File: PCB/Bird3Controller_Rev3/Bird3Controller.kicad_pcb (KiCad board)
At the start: 2 copper layers, 43 x 108 mm, 69 parts, among them IC1 M24C08-RMN6TP, IC2 AP63203WU-7, J1 Bird 3 24-pin Connector, J2 TXW154028S0 Connector, J3 87832-2220, J4 Adafruit USB-C Breakout, Q1 2N7002A, SW1 SW_Boot, SW2 SW_Reset, U1 ESP32-S3-WROOM-1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

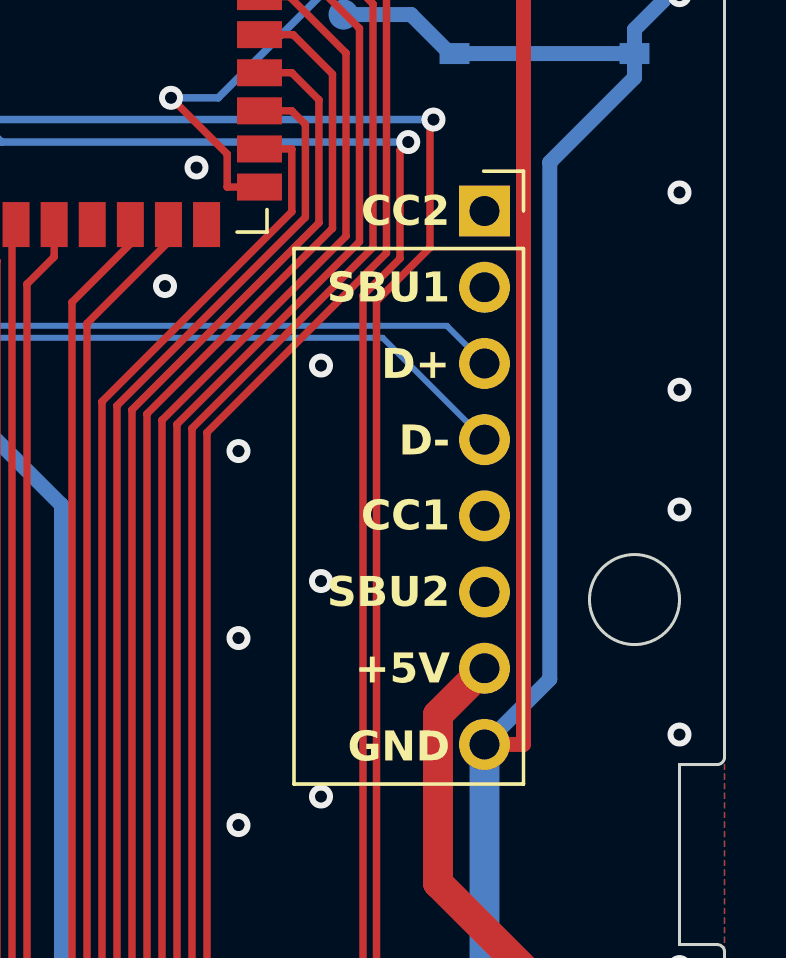
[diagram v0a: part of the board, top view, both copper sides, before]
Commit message: Add `Rating` field, use lower cost VIN cap, add description to most components
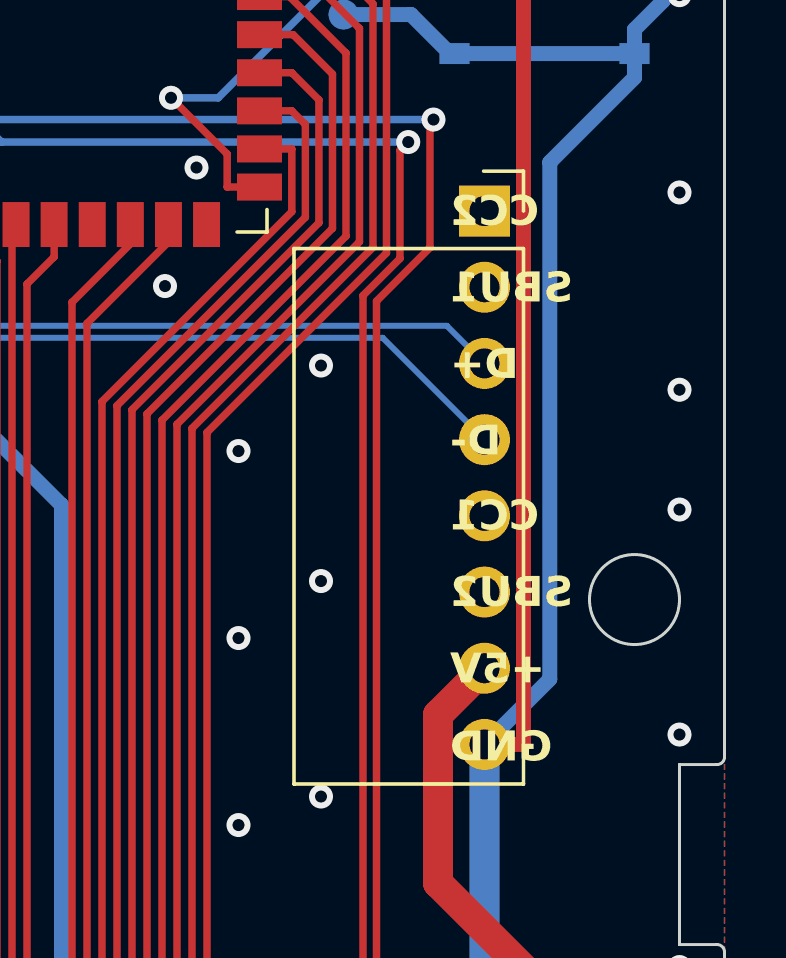
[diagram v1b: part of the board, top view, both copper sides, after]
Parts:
- L2: value MAMK2520H2R2M -> 2u2
